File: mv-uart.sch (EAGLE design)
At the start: 39 parts, among them SW1 DIP_SP6T, U1 IP4234CZ6, U2 CP2105-GM, U3 LDO_SHD_ADJ-AP2127K-ADJ, X1 MINI-USB-SHIELD-UX60-MB-5ST

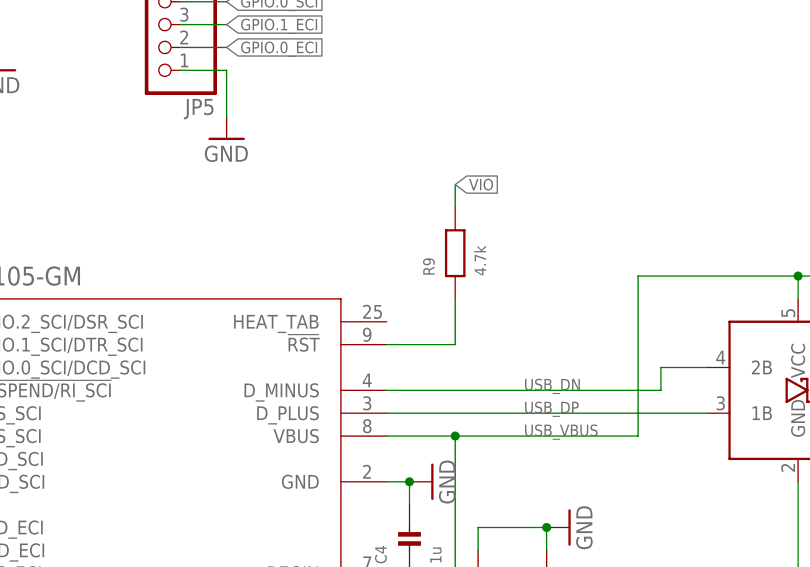
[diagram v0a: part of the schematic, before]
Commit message: first fully routed version of mv-uart
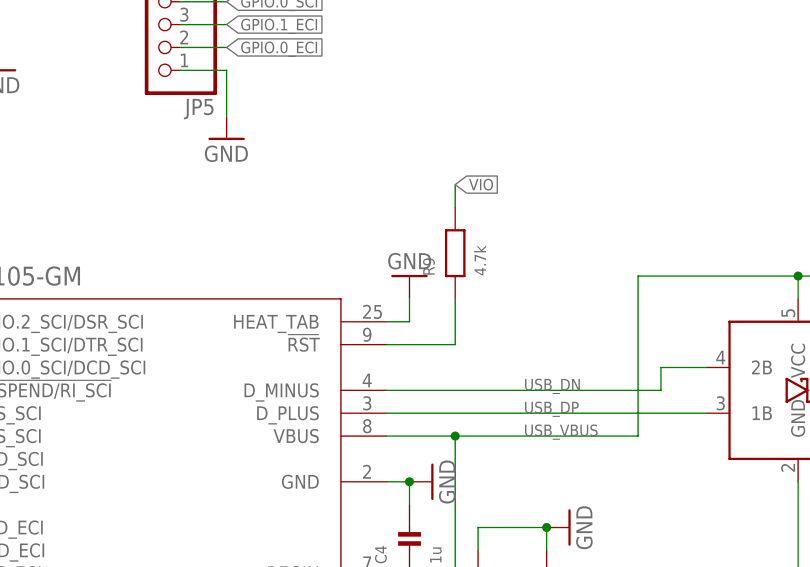
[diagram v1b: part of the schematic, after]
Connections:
- net GND: now also U2.HEAT_TAB
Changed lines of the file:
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@@
 <part name="JP5" library="pinhead" deviceset="PINHD-1X7" device=""/>
 <part name="GND16" library="supply1" deviceset="GND" device=""/>
+<part name="GND17" library="supply1" deviceset="GND" device=""/>
 </parts>
 <sheets>
@@
 <instance part="JP5" gate="A" x="261.62" y="139.7" rot="R180"/>
 <instance part="GND16" gate="1" x="269.24" y="124.46"/>
+<instance part="GND17" gate="1" x="289.56" y="109.22" rot="R180"/>
 </instances>
 <busses>
@@
 <pinref part="GND16" gate="1" pin="GND"/>
 </segment>
-</net>
+<segment>
+<pinref part="U2" gate="A" pin="HEAT_TAB"/>
+<pinref part="GND17" gate="1" pin="GND"/>
+<wire x1="287.02" y1="104.14" x2="289.56" y2="104.14" width="0.1524" layer="91"/>
+<wire x1="289.56" y1="104.14" x2="289.56" y2="106.68" width="0.1524" layer="91"/>
+</segment>
+</net>
